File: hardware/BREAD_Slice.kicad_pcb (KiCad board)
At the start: 2 copper layers, 70 x 100 mm, 69 parts, among them IC1 DS3234S#, J1 I2C_01x04, J2 Conn_01x10_Female, J3 MicroSD_502570-0893, K2 SANYOU_SRD_Form_C, Q1 IRLZ34N, Q2 IRLZ34N, U10 AP2127K-1.8, U2 MQ-x, U3 MQ-x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

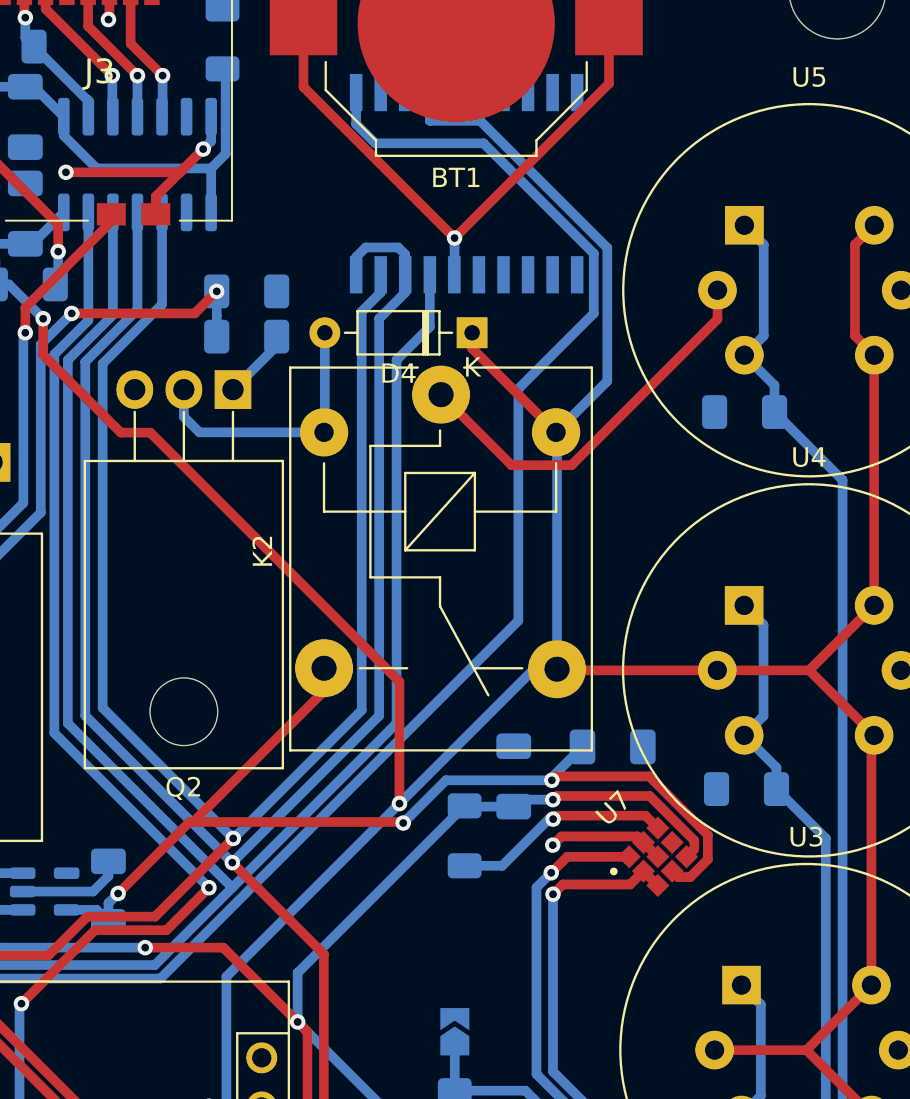
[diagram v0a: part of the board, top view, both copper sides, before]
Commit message: updated parts list and swapped relay to omron var
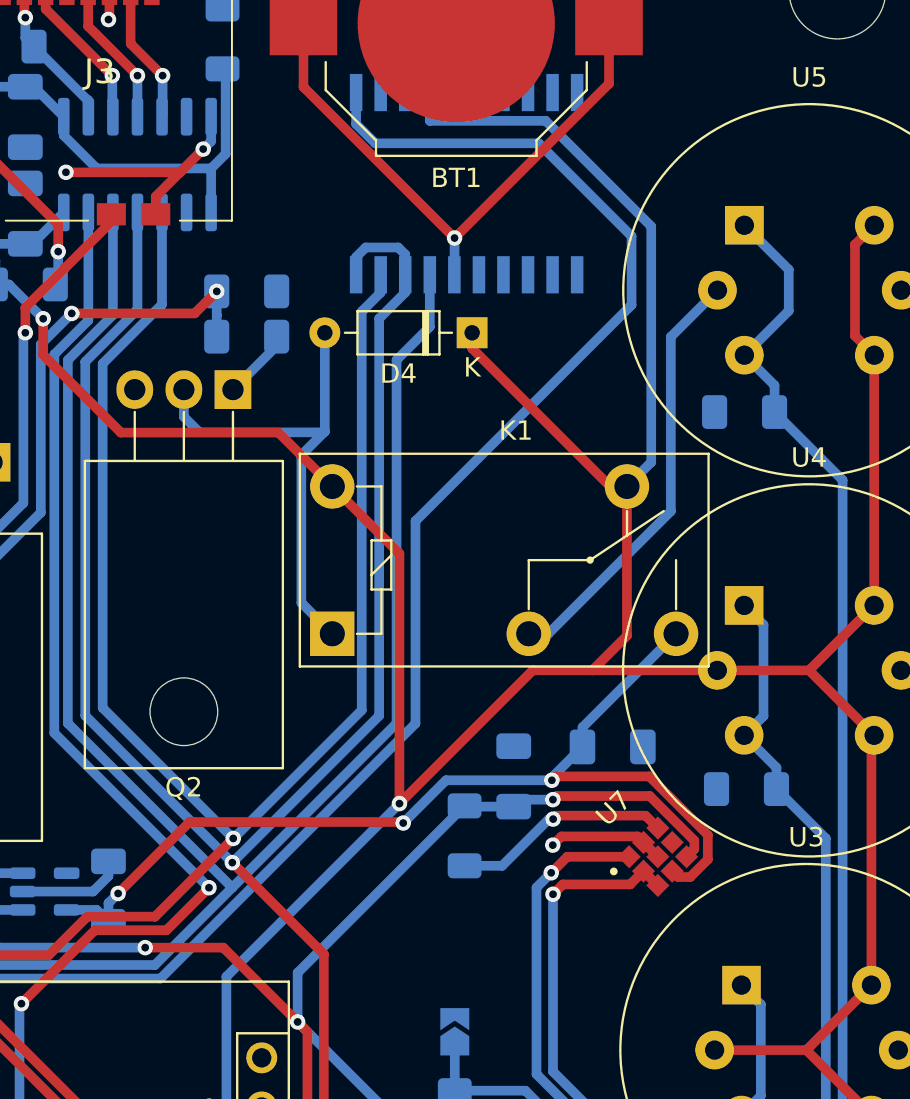
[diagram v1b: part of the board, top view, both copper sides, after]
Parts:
- removed K2: SANYOU_SRD_Form_C, Relay_THT:Relay_SPDT_SANYOU_SRD_Series_Form_C
- added K1: G5Q-1, Relay_THT:Relay_SPDT_Omron-G5Q-1, F.Cu at (161.5, 78.1)
- D2: value H178CAD -> H178CAD
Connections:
- A1 pad 25: /Soft_DAT -> /Soft_CLK
- A1 pad 26: /Soft_CLK -> /Soft_DAT
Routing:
- net +5V: track 346.5 -> 358.3 mm
- net Net-(D4-A): track 14.2 -> 25.8 mm
- net /SS: track 110.7 -> 114.0 mm
- net +1V8: track 55.3 -> 52.4 mm
- net /Vh4: track 20.4 -> 22.4 mm
- net /GS4: track 106.2 -> 107.2 mm

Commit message: checked output for order
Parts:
- moved D4 12.6 mm to (174.5, 73.7), turned to -90 degrees
- moved K1 10.8 mm to (171.2, 82.7), turned to 90 degrees
- moved C7 8.08 mm to (167.1, 92.6), turned to -90 degrees
- moved R2 1.28 mm to (141.2, 65.2)
- moved R3 1.23 mm to (141.2, 63.0)
- moved R10 0.26 mm to (168.5, 88.7), turned to 0 degrees
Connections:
- A1 pad 25: /Soft_CLK -> /Soft_DAT
- A1 pad 26: /Soft_DAT -> /Soft_CLK
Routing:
- net +1V8: track 52.4 -> 67.0 mm, vias 3 -> 2
- net GND: track 123.5 -> 111.8 mm
- net Net-(D4-A): track 25.8 -> 34.4 mm, vias 0 -> 1
- net /Vh4: track 22.4 -> 16.5 mm
- net /SS: track 114.0 -> 119.9 mm
- net +5V: track 358.3 -> 352.7 mm, vias 3 -> 2
- net Net-(BZ1--): track 20.9 -> 23.8 mm
- net +3V3: track 141.2 -> 143.6 mm
- net /ENS 160/~{CS}: track 11.3 -> 9.04 mm
- net Net-(Q1-G): track 5.44 -> 6.68 mm
- net /DI: track 132.0 -> 132.7 mm
- net /CS: track 75.4 -> 75.7 mm, vias 2 -> 4
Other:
- board text removed: "${REFERENCE}"
